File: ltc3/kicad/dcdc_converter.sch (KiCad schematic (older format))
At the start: 18 parts, among them U3 PTN78020W

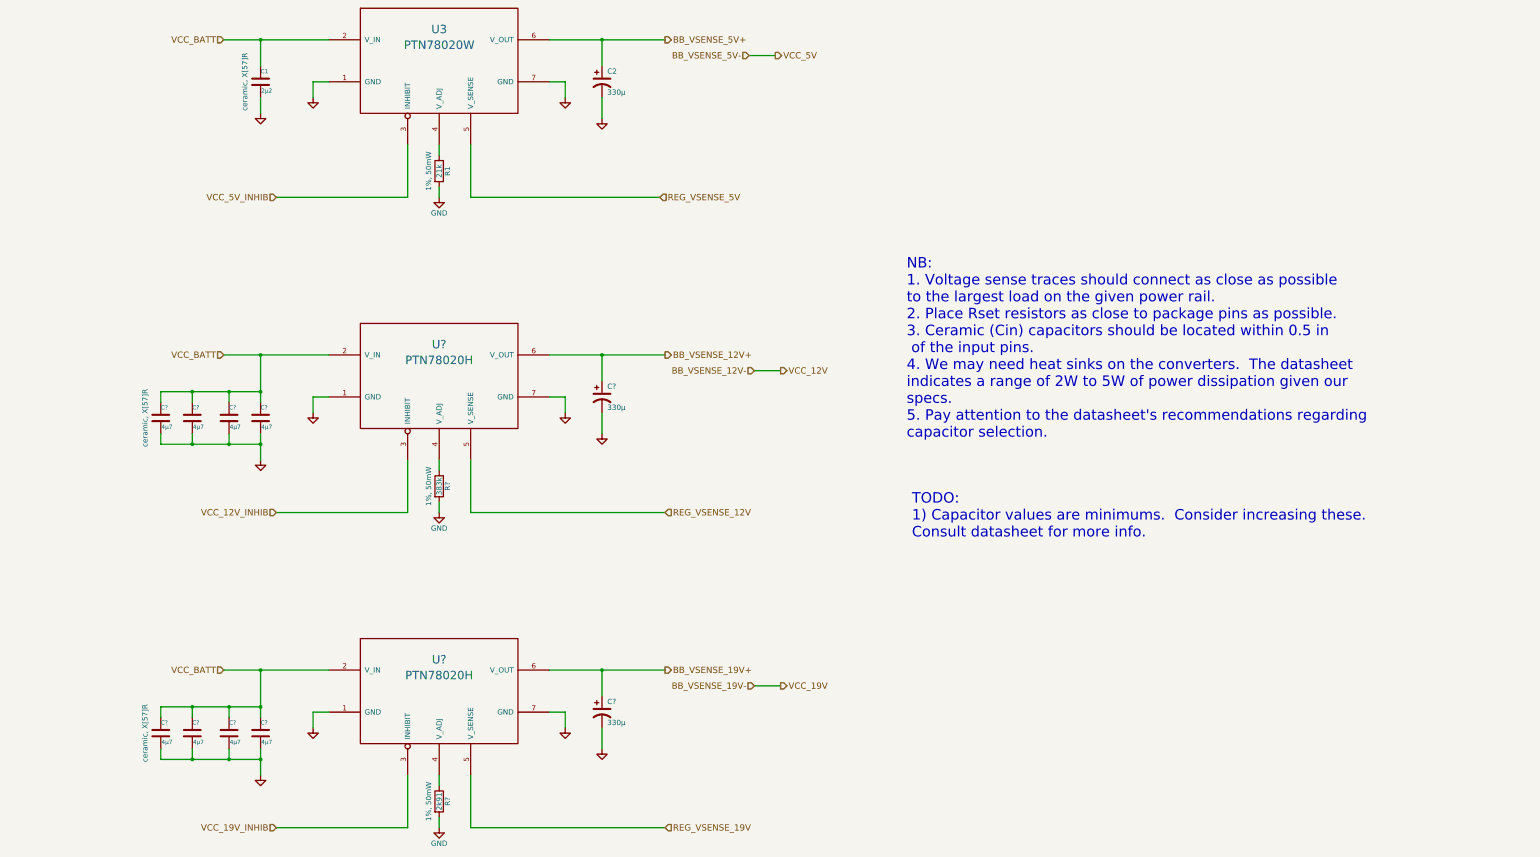
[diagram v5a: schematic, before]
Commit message: Moved voltage/current sense resistors onto DC-DC Converter sheet. From the BeagleBone Cape sheet.  This makes the schematics cleaner, as there are fewer hierarchical pins to keep track of.
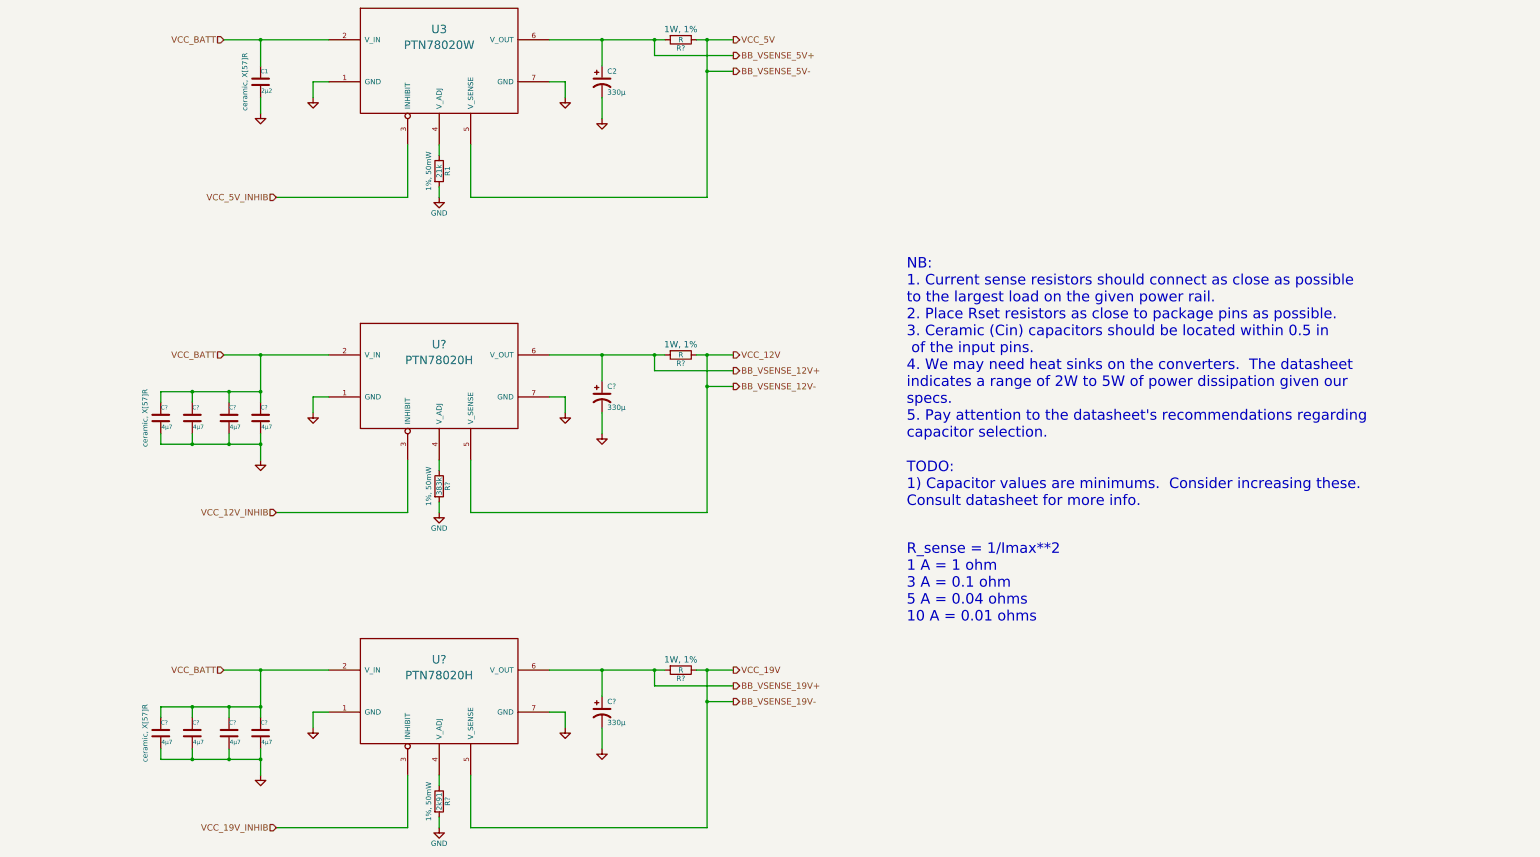
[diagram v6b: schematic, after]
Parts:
- added R? (x3): R, symbol R
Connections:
- net REG_VSENSE_12V is gone; now on net BB_VSENSE_12V-: U?.5 (V_SENSE)
- net REG_VSENSE_19V is gone; now on net BB_VSENSE_19V-: U?.5 (V_SENSE)
- net REG_VSENSE_5V is gone; now on net BB_VSENSE_5V-: U3.5 (V_SENSE)
- net BB_VSENSE_12V+: now also R?.2
- net BB_VSENSE_12V-: now also R?.1
- net BB_VSENSE_19V+: now also R?.2
- net BB_VSENSE_19V-: now also R?.1
- net BB_VSENSE_5V+: now also R?.2
- net BB_VSENSE_5V-: now also R?.1
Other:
- note added: "NB:\n1. Current sense resistors should connect as close as possible\nto the largest load on the given power rail.\n2. Place Rset resistors as close to package pins as possible.\n3. Ceramic (Cin) capacitors should be located within 0.5 in\n of the input pins.\n4. We may need heat sinks on the converters. The datasheet\nindicates a range of 2W to 5W of power dissipation given our\nspecs.\n5. Pay at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"
- note added: "R_sense = 1/Imax**2\n1 A = 1 ohm\n3 A = 0.1 ohm\n5 A = 0.04 ohms\n10 A = 0.01 ohms"
- note removed: "NB:\n1. Voltage sense traces should connect as close as possible\nto the largest load on the given power rail.\n2. Place Rset resistors as close to package pins as possible.\n3. Ceramic (Cin) capacitors should be located within 0.5 in\n of the input pins.\n4. We may need heat sinks on the converters. The datasheet\nindicates a range of 2W to 5W of power dissipation given our\nspecs.\n5. Pay atten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"
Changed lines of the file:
@@
 Comment4 ""
 $EndDescr
-Text HLabel 9200 1950 2    60   Output ~ 0
-VCC_5V
 Text HLabel 3950 1800 0    60   Input ~ 0
 VCC_BATT
@@
 Text HLabel 4450 3300 0    60   Input ~ 0
 VCC_5V_INHIB
-Text HLabel 8150 4800 2    60   Output ~ 0
-BB_VSENSE_12V+
 Text HLabel 3950 4800 0    60   Input ~ 0
 VCC_BATT
@@
 Text HLabel 4450 6300 0    60   Input ~ 0
 VCC_12V_INHIB
-Text HLabel 8150 7800 2    60   Output ~ 0
-BB_VSENSE_19V+
 Text HLabel 3950 7800 0    60   Input ~ 0
 VCC_BATT
@@
 VCC_19V_INHIB
 Text Notes 10450 5600 0    100  ~ 0
-NB:\n1. Voltage sense traces should connect as close as possible\nto the largest load on the given power rail.\n2. Place Rset resistors as close to package pins as possible.\n3. Ceramic (Cin) capacitors should be located within 0.5 in\n of the input pins.\n4. We may need heat sinks on the converters.  The datasheet\nindicates a range of 2W to 5W of power dissipation given our\nspecs.\n5. Pay attention to the datasheet's recommendations regarding\ncapacitor selection.
+NB:\n1. Current sense resistors should connect as close as possible\nto the largest load on the given power rail.\n2. Place Rset resistors as close to package pins as possible.\n3. Ceramic (Cin) capacitors should be located within 0.5 in\n of the input pins.\n4. We may need heat sinks on the converters.  The datasheet\nindicates a range of 2W to 5W of power dissipation given our\nspecs.\n5. Pay attention to the datasheet's recommendations regarding\ncapacitor selection.
 $Comp
 L C C?
@@
 	1    0    0    -1
 $EndComp
-Text Notes 10500 6550 0    100  ~ 0
+Text Notes 10450 6250 0    100  ~ 0
 TODO:\n1) Capacitor values are minimums.  Consider increasing these.\nConsult datasheet for more info.
-Text HLabel 8100 3300 2    60   Input ~ 0
-REG_VSENSE_5V
-Text HLabel 8150 6300 2    60   Input ~ 0
-REG_VSENSE_12V
-Text HLabel 8150 9300 2    60   Input ~ 0
-REG_VSENSE_19V
-Text HLabel 8150 1800 2    60   Output ~ 0
-BB_VSENSE_5V+
-Text HLabel 8950 1950 0    60   Input ~ 0
-BB_VSENSE_5V-
 Wire Wire Line
 	4950 2200 4800 2200
@@
 	7200 2200 7200 2350
 Wire Wire Line
-	7050 1800 8150 1800
-Wire Wire Line
-	3950 1800 4950 1800
+	3950 1800 4300 1800
+Wire Wire Line
+	4300 1800 4950 1800
 Wire Wire Line
 	7550 2050 7550 1800
@@
 	6300 2800 6300 3300
 Wire Wire Line
-	6300 3300 8100 3300
+	6300 3300 8550 3300
 Wire Wire Line
 	4950 5200 4800 5200
@@
 	7200 5200 7200 5350
 Wire Wire Line
-	7050 4800 8150 4800
-Wire Wire Line
-	3950 4800 4950 4800
+	3950 4800 4300 4800
+Wire Wire Line
+	4300 4800 4950 4800
 Wire Wire Line
 	7550 5050 7550 4800
@@
 	7550 5350 7550 5550
 Wire Wire Line
-	4300 5550 4300 5800
-Wire Wire Line
-	4300 4800 4300 5250
+	4300 5550 4300 5650
+Wire Wire Line
+	4300 5650 4300 5800
+Wire Wire Line
+	4300 4800 4300 5150
+Wire Wire Line
+	4300 5150 4300 5250
 Connection ~ 4300 4800
 Wire Wire Line
@@
 	6300 5800 6300 6300
 Wire Wire Line
-	6300 6300 8150 6300
+	6300 6300 8550 6300
 Wire Wire Line
 	4950 8200 4800 8200
@@
 	7200 8200 7200 8350
 Wire Wire Line
-	7050 7800 8150 7800
-Wire Wire Line
-	3950 7800 4950 7800
+	3950 7800 4300 7800
+Wire Wire Line
+	4300 7800 4950 7800
 Wire Wire Line
 	7550 8050 7550 7800
@@
 	6300 8800 6300 9300
 Wire Wire Line
-	6300 9300 8150 9300
+	6300 9300 8550 9300
 Wire Wire Line
 	4000 5150 4000 5250
 Wire Wire Line
-	3350 5150 4300 5150
+	3350 5150 3650 5150
+Wire Wire Line
+	3650 5150 4000 5150
+Wire Wire Line
+	4000 5150 4300 5150
 Connection ~ 4300 5150
 Wire Wire Line
@@
 	4000 5650 4000 5550
 Wire Wire Line
-	3350 5650 4300 5650
+	3350 5650 3650 5650
+Wire Wire Line
+	3650 5650 4000 5650
+Wire Wire Line
+	4000 5650 4300 5650
 Connection ~ 4300 5650
 Wire Wire Line
@@
 Connection ~ 3650 5650
 Wire Wire Line
-	4300 8550 4300 8800
-Wire Wire Line
-	4300 7800 4300 8250
+	4300 8550 4300 8650
+Wire Wire Line
+	4300 8650 4300 8800
+Wire Wire Line
+	4300 7800 4300 8150
+Wire Wire Line
+	4300 8150 4300 8250
 Wire Wire Line
 	4000 8150 4000 8250
 Wire Wire Line
-	3350 8150 4300 8150
+	3350 8150 3650 8150
+Wire Wire Line
+	3650 8150 4000 8150
+Wire Wire Line
+	4000 8150 4300 8150
 Connection ~ 4300 8150
 Wire Wire Line
@@
 	4000 8650 4000 8550
 Wire Wire Line
-	3350 8650 4300 8650
+	3350 8650 3650 8650
+Wire Wire Line
+	3650 8650 4000 8650
+Wire Wire Line
+	4000 8650 4300 8650
 Connection ~ 4300 8650
 Wire Wire Line
@@
 	3350 8550 3350 8650
 Connection ~ 3650 8650
-Wire Wire Line
-	8950 1950 9200 1950
-Text HLabel 9250 4950 2    60   Output ~ 0
+Text HLabel 8800 4800 2    60   Output ~ 0
 VCC_12V
-Text HLabel 9000 4950 0    60   Input ~ 0
+Text HLabel 8800 4950 2    60   Output ~ 0
+BB_VSENSE_12V+
+Text HLabel 8800 5100 2    60   Output ~ 0
 BB_VSENSE_12V-
 Wire Wire Line
-	9000 4950 9250 4950
-Text HLabel 9250 7950 2    60   Output ~ 0
+	7050 4800 7550 4800
+Wire Wire Line
+	7550 4800 8050 4800
+Wire Wire Line
+	8050 4800 8150 4800
+$Comp
+L R R?
+U 1 1 55B2C245
+P 8300 4800
+F 0 "R?" V 8380 4800 50  0000 C CNN
+F 1 "R" V 8300 4800 50  0000 C CNN
+F 2 "" V 8230 4800 30  0000 C CNN
+F 3 "" H 8300 4800 30  0000 C CNN
+F 4 "1W, 1%" V 8200 4800 60  0000 C CNN "Note"
+	1    8300 4800
+	0    1    1    0
+$EndComp
+Wire Wire Line
+	8450 4800 8550 4800
+Wire Wire Line
+	8550 4800 8800 4800
+Wire Wire Line
+	8550 6300 8550 5100
+Wire Wire Line
+	8550 5100 8550 4800
+Connection ~ 8550 4800
+Wire Wire Line
+	8800 4950 8050 4950
+Wire Wire Line
+	8050 4950 8050 4800
+Connection ~ 8050 4800
+Wire Wire Line
+	8800 5100 8550 5100
+Connection ~ 8550 5100
+Wire Wire Line
+	7050 1800 7550 1800
+Connection ~ 8550 2100
+Wire Wire Line
+	8800 2100 8550 2100
+Connection ~ 8050 1800
+Wire Wire Line
+	8050 1950 8050 1800
+Wire Wire Line
+	8800 1950 8050 1950
+Connection ~ 8550 1800
+Wire Wire Line
+	8550 2100 8550 1800
+Wire Wire Line
+	8550 3300 8550 2100
+Wire Wire Line
+	8550 1800 8800 1800
+Wire Wire Line
+	8450 1800 8550 1800
+$Comp
+L R R?
+U 1 1 55B297AA
+P 8300 1800
+F 0 "R?" V 8380 1800 50  0000 C CNN
+F 1 "R" V 8300 1800 50  0000 C CNN
+F 2 "" V 8230 1800 30  0000 C CNN
+F 3 "" H 8300 1800 30  0000 C CNN
+F 4 "1W, 1%" V 8200 1800 60  0000 C CNN "Note"
+	1    8300 1800
+	0    1    1    0
+$EndComp
+Wire Wire Line
+	8050 1800 8150 1800
+Wire Wire Line
+	7550 1800 8050 1800
+Text HLabel 8800 2100 2    60   Output ~ 0
+BB_VSENSE_5V-
+Text HLabel 8800 1950 2    60   Output ~ 0
+BB_VSENSE_5V+
+Text HLabel 8800 1800 2    60   Output ~ 0
+VCC_5V
+Text HLabel 8800 7800 2    60   Output ~ 0
 VCC_19V
-Text HLabel 9000 7950 0    60   Input ~ 0
+Text HLabel 8800 7950 2    60   Output ~ 0
+BB_VSENSE_19V+
+Text HLabel 8800 8100 2    60   Output ~ 0
 BB_VSENSE_19V-
 Wire Wire Line
-	9000 7950 9250 7950
+	7050 7800 7550 7800
+Wire Wire Line
+	7550 7800 8050 7800
+Wire Wire Line
+	8050 7800 8150 7800
+$Comp
+L R R?
+U 1 1 55B2D265
+P 8300 7800
+F 0 "R?" V 8380 7800 50  0000 C CNN
+F 1 "R" V 8300 7800 50  0000 C CNN
+F 2 "" V 8230 7800 30  0000 C CNN
+F 3 "" H 8300 7800 30  0000 C CNN
+F 4 "1W, 1%" V 8200 7800 60  0000 C CNN "Note"
+	1    8300 7800
+	0    1    1    0
+$EndComp
+Wire Wire Line
+	8450 7800 8550 7800
+Wire Wire Line
+	8550 7800 8800 7800
+Wire Wire Line
+	8550 9300 8550 8100
+Wire Wire Line
+	8550 8100 8550 7800
+Connection ~ 8550 7800
+Wire Wire Line
+	8800 7950 8050 7950
+Wire Wire Line
+	8050 7950 8050 7800
+Connection ~ 8050 7800
+Wire Wire Line
+	8800 8100 8550 8100
+Connection ~ 8550 8100
+Text Notes 10450 7350 0    100  ~ 0
+R_sense = 1/Imax**2\n1 A = 1 ohm\n3 A = 0.1 ohm\n5 A = 0.04 ohms\n10 A = 0.01 ohms
 $EndSCHEMATC

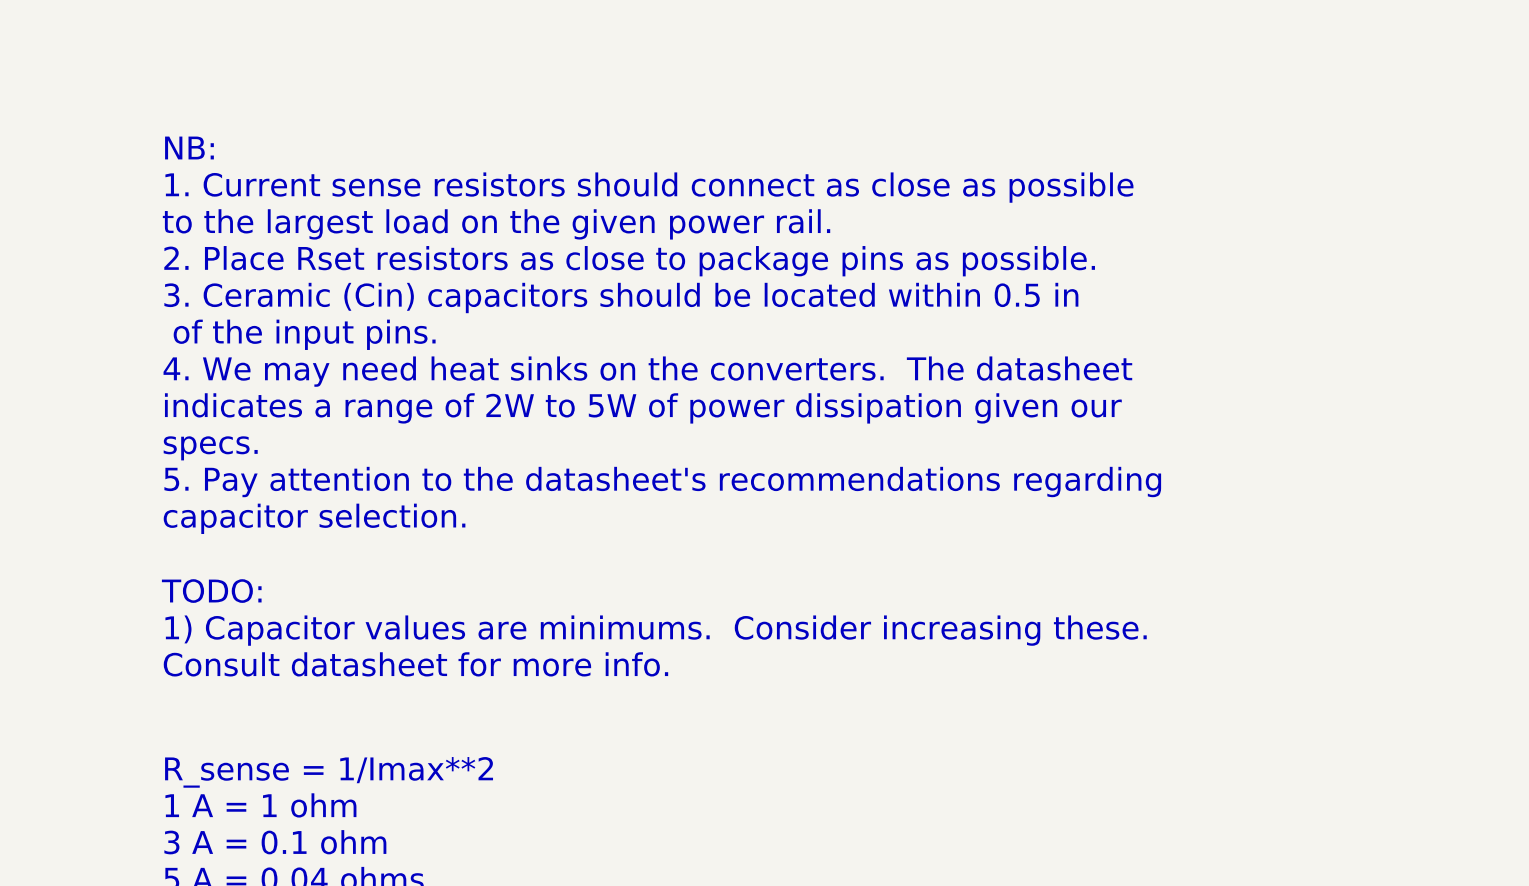
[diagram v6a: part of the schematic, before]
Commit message: Completed first draft of power and temperature sensors.
Updated the design spec accordingly.  Also renamed "Power In" sheet to
"Power Sources".
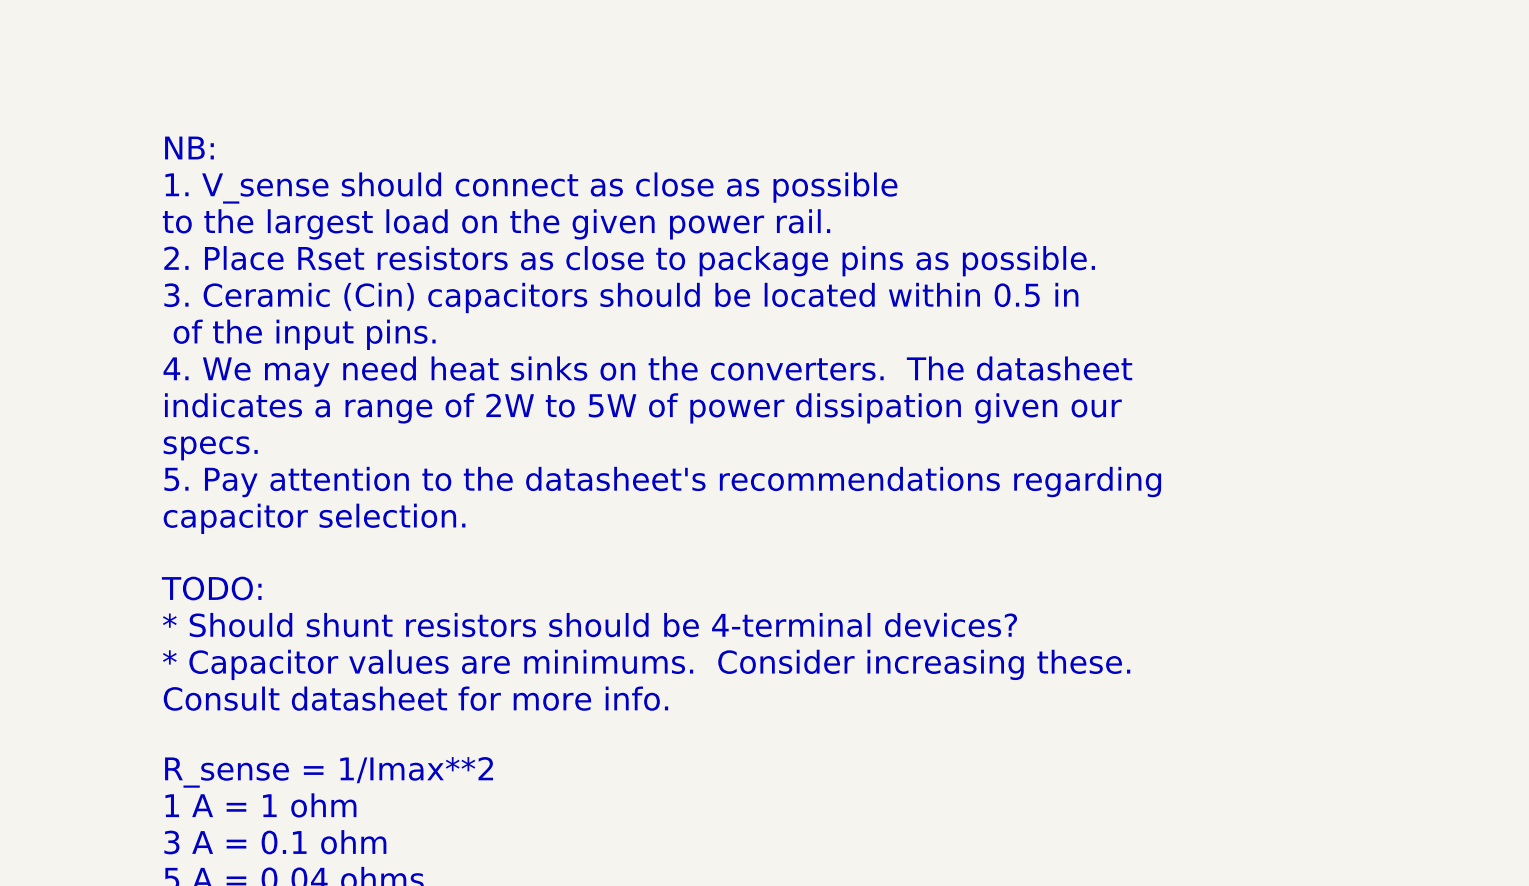
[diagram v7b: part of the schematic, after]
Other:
- note added: "NB:\n1. V_sense should connect as close as possible\nto the largest load on the given power rail.\n2. Place Rset resistors as close to package pins as possible.\n3. Ceramic (Cin) capacitors should be located within 0.5 in\n of the input pins.\n4. We may need heat sinks on the converters. The datasheet\nindicates a range of 2W to 5W of power dissipation given our\nspecs.\n5. Pay attention to the d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"
- note added: "TODO:\n* Should shunt resistors should be 4-terminal devices?\n* Capacitor values are minimums. Consider increasing these.\nConsult datasheet for more info."
- note removed: "NB:\n1. Current sense resistors should connect as close as possible\nto the largest load on the given power rail.\n2. Place Rset resistors as close to package pins as possible.\n3. Ceramic (Cin) capacitors should be located within 0.5 in\n of the input pins.\n4. We may need heat sinks on the converters. The datasheet\nindicates a range of 2W to 5W of power dissipation given our\nspecs.\n5. Pay at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"
- note removed: "TODO:\n1) Capacitor values are minimums. Consider increasing these.\nConsult datasheet for more info."
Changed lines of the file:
@@
 VCC_19V_INHIB
 Text Notes 10450 5600 0    100  ~ 0
-NB:\n1. Current sense resistors should connect as close as possible\nto the largest load on the given power rail.\n2. Place Rset resistors as close to package pins as possible.\n3. Ceramic (Cin) capacitors should be located within 0.5 in\n of the input pins.\n4. We may need heat sinks on the converters.  The datasheet\nindicates a range of 2W to 5W of power dissipation given our\nspecs.\n5. Pay attention to the datasheet's recommendations regarding\ncapacitor selection.
+NB:\n1. V_sense should connect as close as possible\nto the largest load on the given power rail.\n2. Place Rset resistors as close to package pins as possible.\n3. Ceramic (Cin) capacitors should be located within 0.5 in\n of the input pins.\n4. We may need heat sinks on the converters.  The datasheet\nindicates a range of 2W to 5W of power dissipation given our\nspecs.\n5. Pay attention to the datasheet's recommendations regarding\ncapacitor selection.
 $Comp
 L C C?
@@
 	1    0    0    -1
 $EndComp
-Text Notes 10450 6250 0    100  ~ 0
-TODO:\n1) Capacitor values are minimums.  Consider increasing these.\nConsult datasheet for more info.
+Text Notes 10450 6400 0    100  ~ 0
+TODO:\n* Should shunt resistors should be 4-terminal devices?\n* Capacitor values are minimums.  Consider increasing these.\nConsult datasheet for more info.
 Wire Wire Line
 	4950 2200 4800 2200
